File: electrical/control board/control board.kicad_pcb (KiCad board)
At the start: 4 copper layers, 147.6 x 143.9 mm, 71 parts, among them J1 analog_extra, J10 Motor_2, J11 Motor_3, J12 Motor_4, J13 Motor_5, J14 Motor_6, J15 Motor_7, J16 Motor_8, J2 Programming_Header, J3 USB_B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

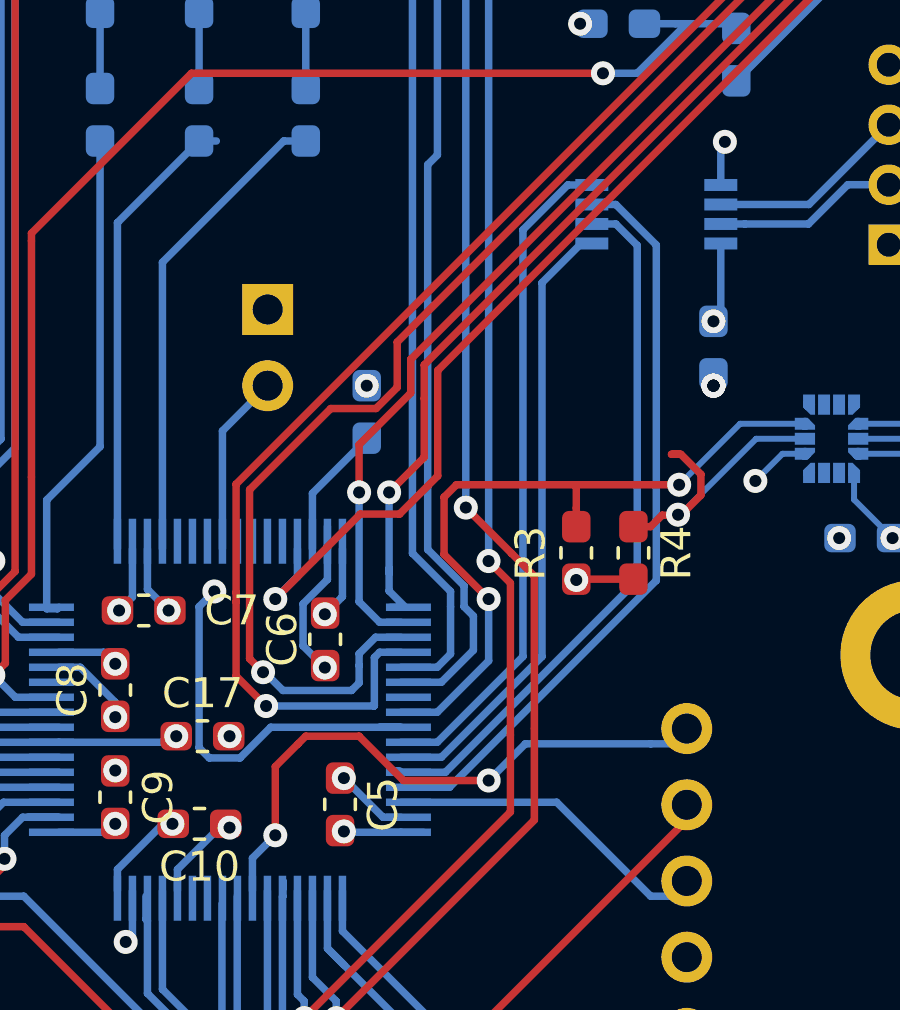
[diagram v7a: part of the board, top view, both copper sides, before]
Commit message: rerouted some things
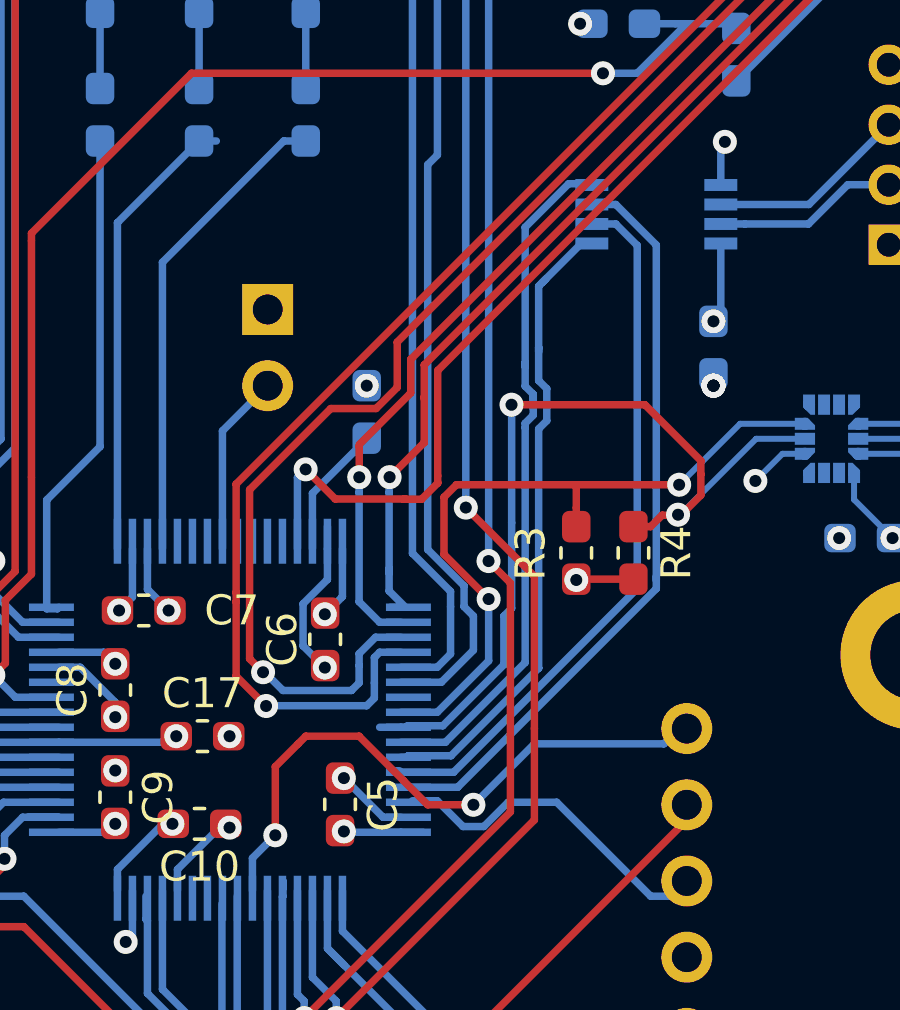
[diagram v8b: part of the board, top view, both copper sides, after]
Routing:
- net /ICM_SCL: track 23.6 -> 30.1 mm
- net /SWITCH_A: track 57.0 -> 56.0 mm
- net /SENSOR_TX: track 22.7 -> 23.6 mm
- net /SENSOR_RX: track 20.8 -> 21.5 mm
- net /JTDO: track 19.7 -> 20.3 mm
